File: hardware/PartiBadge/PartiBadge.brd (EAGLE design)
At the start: 101.6 x 101.6 mm, 24 parts, among them J1 I2C, J2 Supply

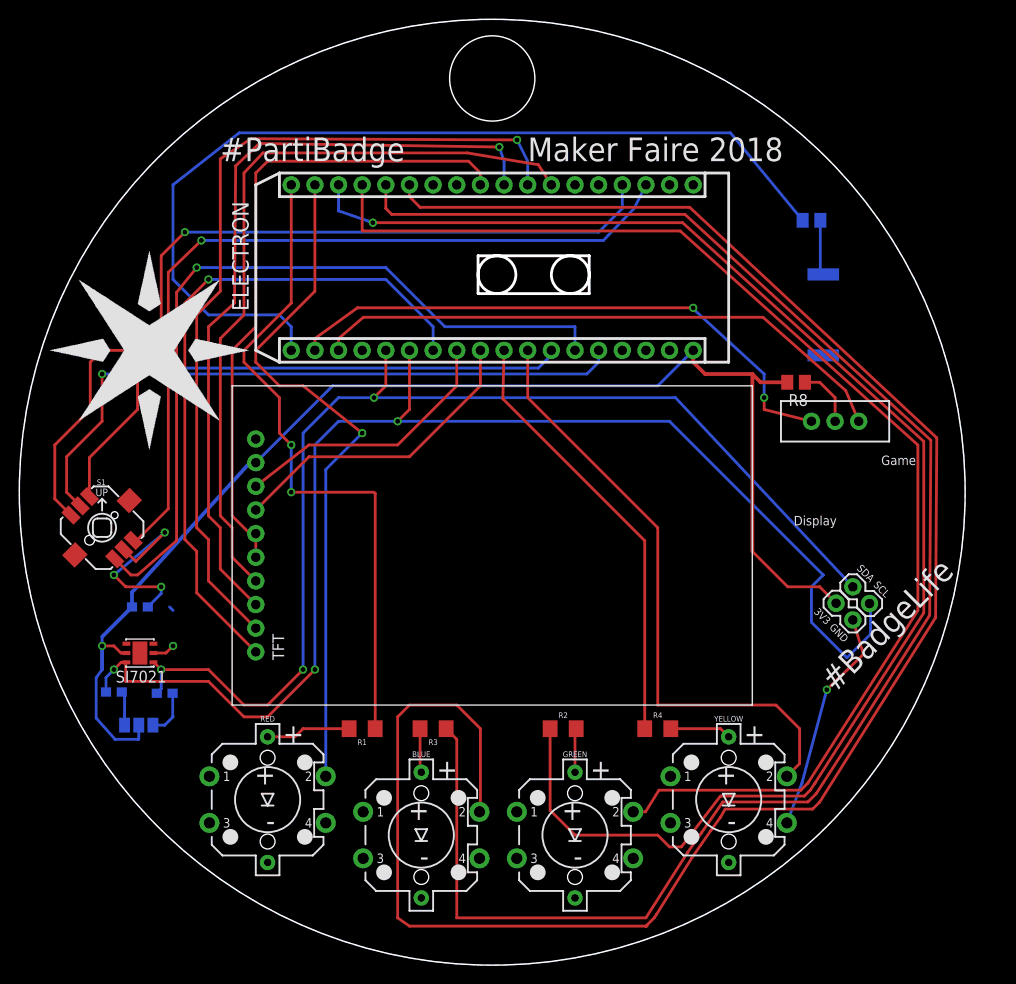
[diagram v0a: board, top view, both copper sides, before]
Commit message: route and via cleanup; closes #11
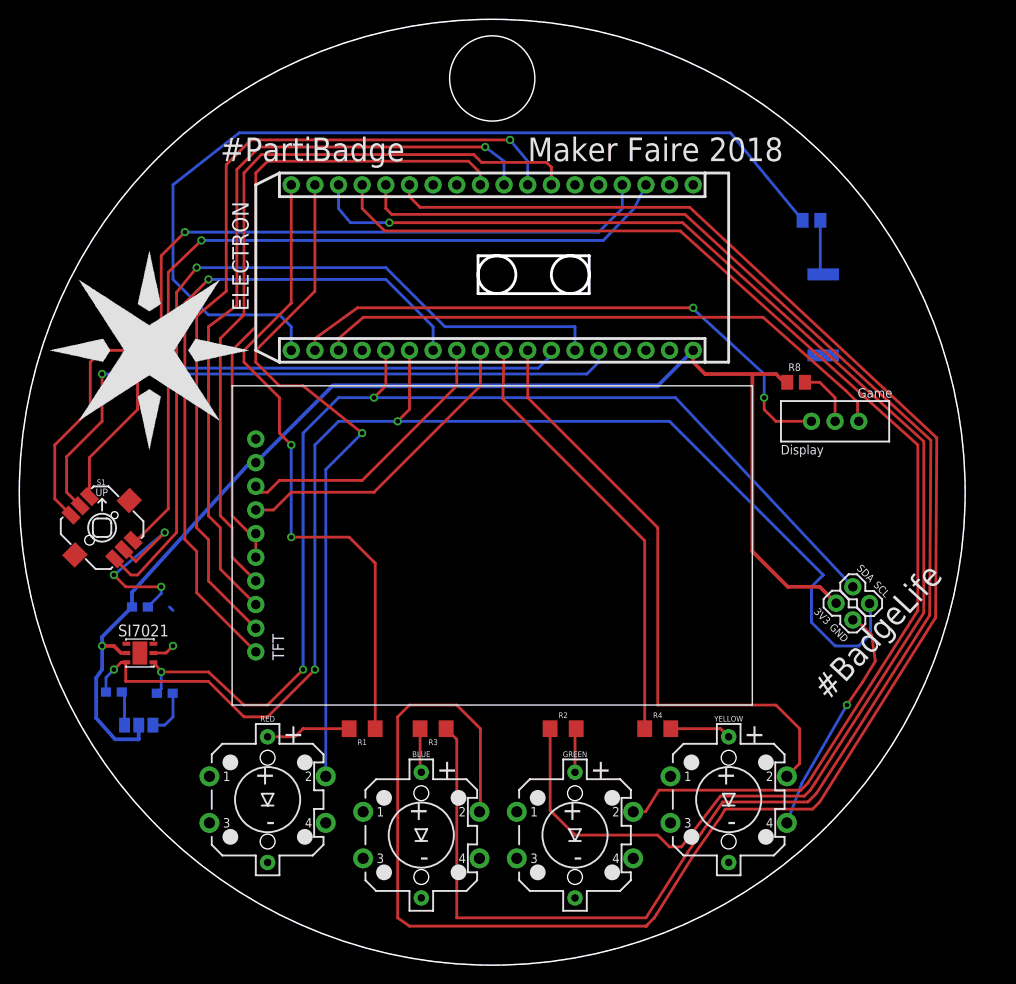
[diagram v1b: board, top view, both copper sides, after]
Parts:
- added U$1: (no value), particle-spark:SPARK#PNG
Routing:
- net LED_RED: track 71.6 -> 70.0 mm
- net N$6: track 133.6 -> 132.2 mm
- net SPI_MOSI: track 81.7 -> 82.8 mm
- net GND: track 48.9 -> 50.0 mm
- net SCL: track 143.2 -> 142.2 mm
- net TFT_RST: track 29.6 -> 30.4 mm
- net SPI_SCK: track 83.9 -> 83.1 mm
- net SPI_MISO: track 91.7 -> 91.0 mm

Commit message: rear-side logo positioning
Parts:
- moved U$1 0.80 mm to (54.9, 36.1)
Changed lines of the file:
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@@
 <wire x1="51.816" y1="78.486" x2="63.754" y2="78.486" width="0.3048" layer="46"/>
 <wire x1="63.754" y1="78.486" x2="63.754" y2="82.55" width="0.3048" layer="46"/>
-<text x="55.88" y="54.61" size="3.81" layer="22" font="vector" ratio="18" rot="MR0" align="center">Designed by
+<text x="55.753" y="55.118" size="3.81" layer="22" font="vector" ratio="18" rot="MR0" align="center">Designed by
 The Particle Team
 http://Particle.io</text>
@@
 <attribute name="VALUE" x="86.868" y="67.818" size="0.8128" layer="27" ratio="18" rot="R180"/>
 </element>
-<element name="U$1" library="particle-spark" package="SPARK#PNG" value="" x="54.61" y="36.83" rot="MR90"/>
+<element name="U$1" library="particle-spark" package="SPARK#PNG" value="" x="54.864" y="36.068" rot="MR90"/>
 </elements>
 <signals>

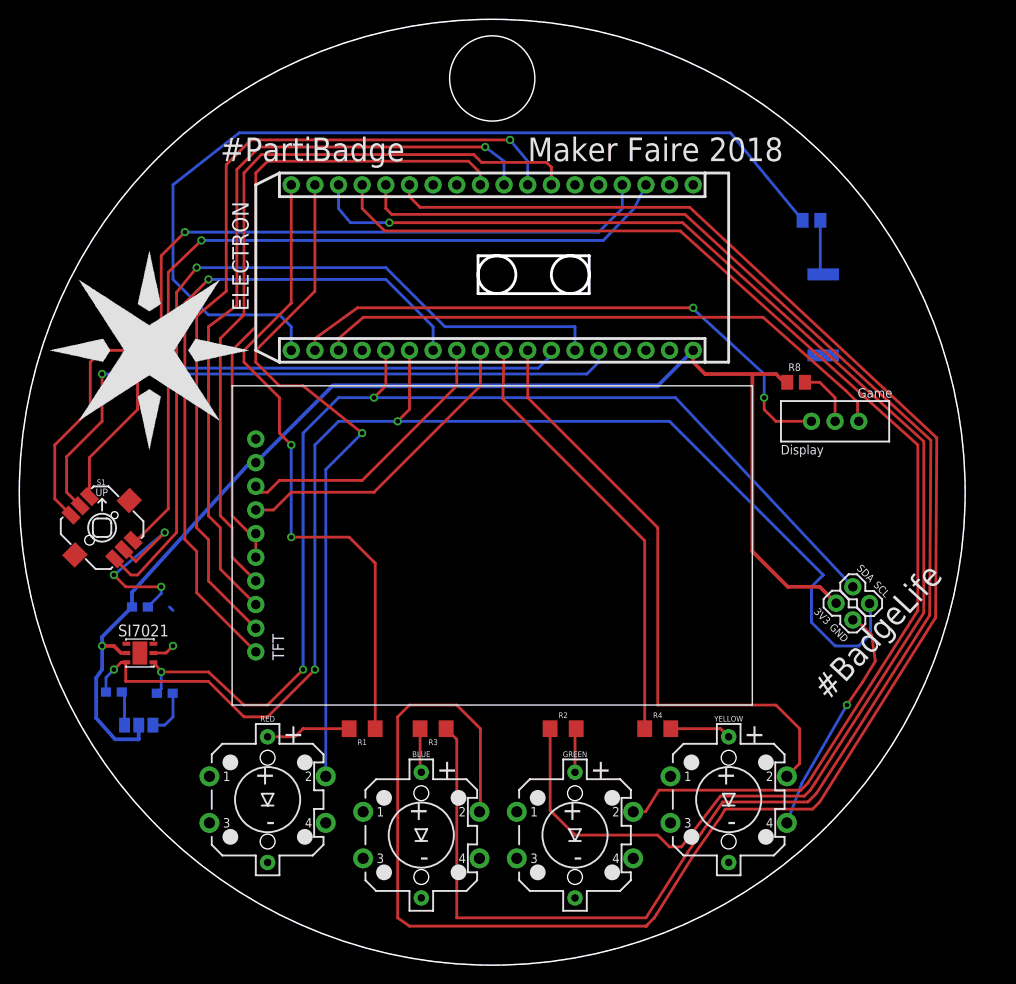
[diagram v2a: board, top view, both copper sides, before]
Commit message: fix right-angle routes; closes #13
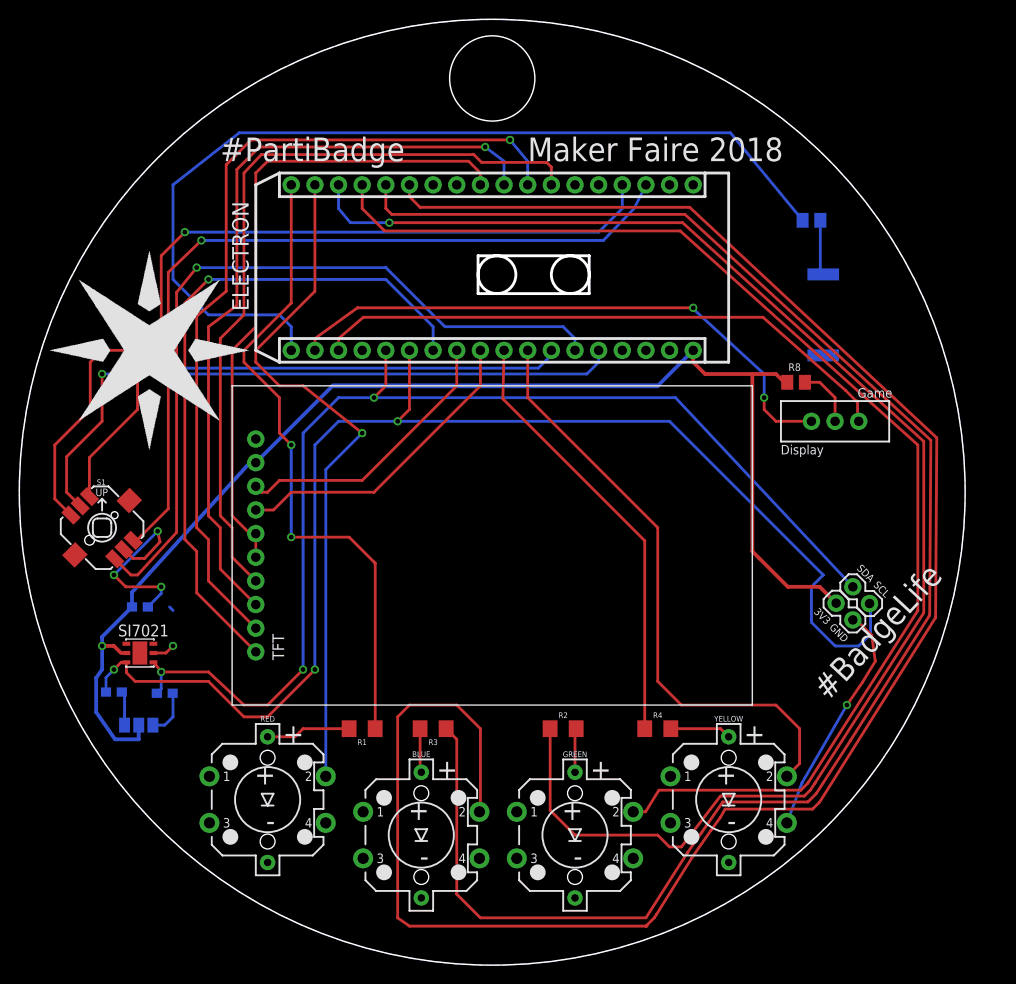
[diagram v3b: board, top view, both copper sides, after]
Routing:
- net LED_BLUE: track 178.8 -> 177.3 mm
- net BUTTON_YELLOW: track 65.9 -> 64.4 mm
- net DOWN: track 84.4 -> 83.6 mm
- net SCL: track 142.2 -> 141.6 mm
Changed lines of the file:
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@@
 <drawing>
 <settings>
-<setting alwaysvectorfont="yes"/>
+<setting alwaysvectorfont="no"/>
 <setting verticaltext="up"/>
 </settings>
@@
 <vertex x="2.54" y="57.15" curve="-90"/>
 </polygon>
-<wire x1="13.781128125" y1="50.98886875" x2="15.05113125" y2="49.71886875" width="0.3048" layer="1"/>
-<wire x1="15.05113125" y1="49.71886875" x2="18.161" y2="52.832" width="0.3048" layer="1"/>
-<via x="18.161" y="52.832" extent="1-16" drill="0.5"/>
+<via x="17.399" y="52.959" extent="1-16" drill="0.5"/>
 <wire x1="16.944" y1="39.878" x2="18.288" y2="39.878" width="0.3048" layer="1"/>
 <wire x1="18.288" y1="39.878" x2="19.05" y2="40.64" width="0.3048" layer="1"/>
@@
 <wire x1="13.97" y1="46.99" x2="12.7" y2="48.26" width="0.3048" layer="1"/>
 <via x="12.7" y="48.26" extent="1-16" drill="0.5"/>
-<wire x1="12.7" y1="48.26" x2="18.161" y2="52.832" width="0.3048" layer="16"/>
+<wire x1="12.7" y1="48.26" x2="17.399" y2="52.959" width="0.3048" layer="16"/>
 <wire x1="91.44" y1="34.29" x2="93.091" y2="36.703" width="0.3048" layer="1"/>
 <wire x1="93.091" y1="36.703" x2="94.488" y2="38.989" width="0.3048" layer="1"/>
@@
 <wire x1="94.107" y1="41.783" x2="92.456" y2="43.434" width="0.3048" layer="1"/>
 <wire x1="92.456" y1="43.434" x2="92.075" y2="43.434" width="0.3048" layer="1"/>
+<wire x1="13.781128125" y1="50.98886875" x2="14.731996875" y2="50.038" width="0.3048" layer="1"/>
+<wire x1="16.002" y1="50.038" x2="17.653" y2="51.816" width="0.3048" layer="1"/>
+<wire x1="17.653" y1="51.816" x2="17.399" y2="52.959" width="0.3048" layer="1"/>
+<wire x1="14.731996875" y1="50.038" x2="16.002" y2="50.038" width="0.3048" layer="1"/>
 </signal>
 <signal name="N$2">
@@
 <wire x1="11.43" y1="40.64" x2="11.43" y2="38.1" width="0.4064" layer="16"/>
 <wire x1="11.43" y1="38.1" x2="10.795" y2="37.211" width="0.4064" layer="16"/>
-<wire x1="10.795" y1="37.211" x2="10.795" y2="32.893" width="0.4064" layer="16"/>
-<wire x1="10.795" y1="32.893" x2="12.827" y2="30.607" width="0.4064" layer="16"/>
+<wire x1="10.795" y1="37.211" x2="10.795" y2="33.528" width="0.4064" layer="16"/>
+<wire x1="10.795" y1="33.528" x2="12.827" y2="30.607" width="0.4064" layer="16"/>
 <wire x1="12.827" y1="30.607" x2="15.367" y2="30.607" width="0.4064" layer="16"/>
 <wire x1="15.367" y1="30.607" x2="15.367" y2="32.131" width="0.4064" layer="16"/>
@@
 <contactref element="R3" pad="1"/>
 <wire x1="48.39" y1="31.75" x2="49.53" y2="30.61" width="0.3048" layer="1"/>
-<wire x1="49.53" y1="30.61" x2="49.53" y2="11.43" width="0.3048" layer="1"/>
-<wire x1="49.53" y1="11.43" x2="69.85" y2="11.43" width="0.3048" layer="1"/>
+<wire x1="49.53" y1="30.61" x2="49.53" y2="13.97" width="0.3048" layer="1"/>
 <wire x1="74.295" y1="18.415" x2="75.819" y2="20.574" width="0.3048" layer="1"/>
 <wire x1="75.819" y1="20.574" x2="78.105" y2="23.876" width="0.3048" layer="1"/>
 <wire x1="78.105" y1="23.876" x2="87.249" y2="23.876" width="0.3048" layer="1"/>
-<wire x1="69.85" y1="11.43" x2="74.295" y2="18.415" width="0.3048" layer="1"/>
+<wire x1="74.295" y1="18.415" x2="69.85" y2="11.43" width="0.3048" layer="1"/>
 <wire x1="87.249" y1="23.876" x2="88.138" y2="24.765" width="0.3048" layer="1"/>
 <wire x1="88.138" y1="24.765" x2="91.821" y2="30.48" width="0.3048" layer="1"/>
@@
 <wire x1="41.91" y1="87.63" x2="41.91" y2="90.17" width="0.3048" layer="1"/>
 <wire x1="74.041" y1="86.995" x2="42.545" y2="86.995" width="0.3048" layer="1"/>
+<wire x1="69.85" y1="11.43" x2="52.07" y2="11.43" width="0.3048" layer="1"/>
+<wire x1="52.07" y1="11.43" x2="49.53" y2="13.97" width="0.3048" layer="1"/>
 </signal>
 <signal name="N$8">
@@
 <wire x1="86.36" y1="28" x2="86.36" y2="31.75" width="0.3048" layer="1"/>
 <wire x1="86.36" y1="31.75" x2="83.82" y2="34.29" width="0.3048" layer="1"/>
-<wire x1="83.82" y1="34.29" x2="71.12" y2="34.29" width="0.3048" layer="1"/>
-<wire x1="71.12" y1="34.29" x2="71.12" y2="53.34" width="0.3048" layer="1"/>
 <wire x1="71.12" y1="53.34" x2="57.15" y2="67.31" width="0.3048" layer="1"/>
+<wire x1="83.82" y1="34.29" x2="73.66" y2="34.29" width="0.3048" layer="1"/>
+<wire x1="73.66" y1="34.29" x2="71.12" y2="36.83" width="0.3048" layer="1"/>
+<wire x1="71.12" y1="36.83" x2="71.12" y2="53.34" width="0.3048" layer="1"/>
 </signal>
 <signal name="SDA">
@@
 <via x="43.18" y="64.77" extent="1-16" drill="0.5"/>
 <wire x1="14.044" y1="38.878" x2="13.97" y2="38.804" width="0.3048" layer="1"/>
-<wire x1="13.97" y1="38.804" x2="13.97" y2="36.83" width="0.3048" layer="1"/>
-<wire x1="13.97" y1="36.83" x2="22.86" y2="36.83" width="0.3048" layer="1"/>
 <wire x1="22.86" y1="36.83" x2="26.67" y2="33.02" width="0.3048" layer="1"/>
 <wire x1="26.67" y1="33.02" x2="29.21" y2="33.02" width="0.3048" layer="1"/>
@@
 <wire x1="92.71" y1="40.64" x2="90.17" y2="40.64" width="0.3048" layer="16"/>
 <wire x1="90.17" y1="40.64" x2="87.63" y2="43.18" width="0.3048" layer="16"/>
+<wire x1="14.044" y1="38.878" x2="14.044" y2="37.772" width="0.3048" layer="1"/>
+<wire x1="14.044" y1="37.772" x2="14.986" y2="36.83" width="0.3048" layer="1"/>
+<wire x1="14.986" y1="36.83" x2="22.86" y2="36.83" width="0.3048" layer="1"/>
 </signal>
 <signal name="N$11">
@@
 <wire x1="21.59" y1="81.28" x2="41.91" y2="81.28" width="0.3048" layer="16"/>
 <wire x1="41.91" y1="81.28" x2="48.26" y2="74.93" width="0.3048" layer="16"/>
-<wire x1="48.26" y1="74.93" x2="62.23" y2="74.93" width="0.3048" layer="16"/>
-<wire x1="62.23" y1="74.93" x2="62.23" y2="72.39" width="0.3048" layer="16"/>
 <wire x1="12.791178125" y1="49.99891875" x2="14.530096875" y2="48.26" width="0.3048" layer="1"/>
 <wire x1="14.530096875" y1="48.26" x2="15.24" y2="48.26" width="0.3048" layer="1"/>
@@
 <wire x1="19.431" y1="52.832" x2="19.431" y2="78.613" width="0.3048" layer="1"/>
 <wire x1="19.431" y1="78.613" x2="21.59" y2="81.28" width="0.3048" layer="1"/>
+<wire x1="48.26" y1="74.93" x2="60.96" y2="74.93" width="0.3048" layer="16"/>
+<wire x1="60.96" y1="74.93" x2="62.23" y2="73.66" width="0.3048" layer="16"/>
+<wire x1="62.23" y1="73.66" x2="62.23" y2="72.39" width="0.3048" layer="16"/>
 </signal>
 <signal name="LEFT">
